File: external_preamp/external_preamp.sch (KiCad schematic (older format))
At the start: 2 parts

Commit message: Monday night hacking
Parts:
- added C1, C7: 0.68uF, symbol Device:C
- added C10, C3: 4.7uF, symbol Device:C
- added C11, C4: 25uF, symbol Device:C
- added C12, C20, C21, C5: 0.022uF, symbol Device:C
- added C13, C15, C17, C18: 220uF 450V, symbol Device:C
- added C14, C6: 47uF 450V, symbol Device:CP
- added C16: C, symbol Device:C
- added C19: 470pF, symbol Device:C
- added C2, C9: 1uF, symbol Device:C
- added C22: 0.1uF, symbol Device:C
- added C8: 0.01uF, symbol Device:C
- added D1, D2, D4, D5: 1N4007, symbol pspice:DIODE
- added D3: LED, symbol Device:LED
- added F1: F1494-ND, symbol Device:Fuse
- added J1: IEC_SOCKET, symbol yga1:IEC_SOCKET
- added J2: IN, symbol yga1:jack_0.25in_mono_sw
- added J3: OUT, symbol yga1:jack_0.25in_mono_sw
- added R10: 10K 1W, symbol Device:R
- added R11: 3K 2W, symbol Device:R
- added R12, R4, R6, R9: 220K, symbol Device:R
- added R13, R15, R18, R2, R20, R7: 100K, symbol Device:R
- added R14, R19, R3, R8: 820, symbol Device:R
- added R16: 100K 2W, symbol Device:R
- added R17: 33K, symbol Device:R
- added R5: R, symbol Device:R
- added RV1, RV4: 100K, symbol Device:R_POT
- added RV10, RV8: 1M LOG, symbol Device:R_POT
- added RV2, RV5: 5K, symbol Device:R_POT
- added RV3, RV6: 500K LOG, symbol Device:R_POT
- added RV7: 250K LN, symbol Device:R_POT
- added RV9: 100K LN, symbol Device:R_POT
- added SW1: EG4810-ND, symbol Switch:SW_SPST
- added SW2, SW4: SW_SP4T, symbol yga1:SW_SP4T
- added SW3, SW5: SW_SPST, symbol Switch:SW_SPST
- added T1: HM4995-ND, symbol Device:Transformer_1P_2S
- added unit 2 of V1
- added V2, V3: 12AX7A, symbol external_preamp-rescue:12AX7A
- R1: renamed from R?; value R -> 1M; symbol R -> external_preamp-rescue:R
- V1: renamed from V?; symbol 12AX7A -> external_preamp-rescue:12AX7A
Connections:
- net Earth: now also C1.2, C10.2, C11.2, C13.2, C14.2, C15.2, C17.2, C18.2, C2.2, C3.2, C4.2, C6.2, C7.2, C9.2, J1.2 (G), J2.2, J2.3, J3.2, R12.1, R14.2, R15.2, R16.2, R19.2, R20.2, R3.2, R6.1, R8.2, RV10.3, RV3.3, RV6.3, RV9.3
- net at V1.1-UA (A): now also C5.2, R2.2
- net at V1.2-UA (G): now also R1.1, J2.1
- net at V1.3-UA (C): now also RV2.1, SW2.A
- net lf1: now reaches V1.4-UA
- net f2: now reaches V1.9
- net f2: now also D3.1 (K), T1.6 (SD), V1.9, V2.9, V2.9, V3.9, V3.9
- new net: C4.1, SW2.1
- new net: R3.1, RV2.2, RV2.3
- new net: C12.2, R7.2, V1.6-UB (A)
- new net: C8.1, R4.1, R6.2, V1.7-UB (G)
- new net: RV5.1, SW4.A, V1.8-UB (C)
- new net: R13.2, V2.1-UA (A), V2.7-UB (G)
- new net: C16.1, R12.2, R9.1, V2.2-UA (G)
- new net: R14.1, V2.3-UA (C)
- new net: C19.2, R15.1, R17.1, V2.8-UB (C)
- new net: C5.1, RV3.1
- new net: R4.2, RV3.2, SW3.1 (A)
- new net: R2.1, RV1.2, RV1.3
- new net: C3.1, SW2.2
- new net: C2.1, SW2.3
- new net: C1.1, SW2.4
- new net: C14.1, C6.1, R10.2, RV1.1, RV4.1
- new net: C8.2, SW3.2 (B)
- new net: C11.1, SW4.1
- new net: R8.1, RV5.2, RV5.3
- new net: C12.1, RV6.1
- new net: R9.2, RV6.2, SW5.1 (A)
- new net: R7.1, RV4.2, RV4.3
- new net: C10.1, SW4.2
- new net: C9.1, SW4.3
- new net: C7.1, SW4.4
- new net: C16.2, SW5.2 (B)
- new net: C19.1, RV7.1
- new net: C20.2, C21.2, R17.2
- new net: RV10.1, RV7.2
- new net: C20.1, RV7.3, RV8.1, RV8.2
- new net: RV8.3, RV9.1
- new net: C21.1, RV9.2
- new net: R18.2, V3.1-UA (A), V3.7-UB (G)
- new net: R19.1, V3.3-UA (C)
- new net: C22.2, R20.1, V3.8-UB (C)
- new net: C22.1, J3.1
- new net: J1.1 (L), SW1.1 (A)
- new net: J1.3 (N), T1.2 (AB)
- new net: F1.2, SW1.2 (B)
- new net: F1.1, T1.1 (AA)
- new net: D1.2 (A), D4.1 (K), T1.3 (SA)
- new net: D2.2 (A), D5.1 (K), T1.4 (SB)
- new net: D1.1 (K), D2.1 (K)
- new net: C13.1, C15.1, D4.2 (A), D5.2 (A), R11.2
- new net: C17.1, C18.1, R11.1, R16.1
- new net: D3.2 (A), R5.2
- new net B+: R10.1, R13.1, R18.1, V2.6-UB (A), V3.6-UB (A)
- new net f1: R5.1, T1.5 (SC), V1.5-UB, V2.4-UA, V2.5-UB, V3.4-UA, V3.5-UB
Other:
- note added: "300V"
- note added: "6.3V"
- moved on the sheet: R1, V1A

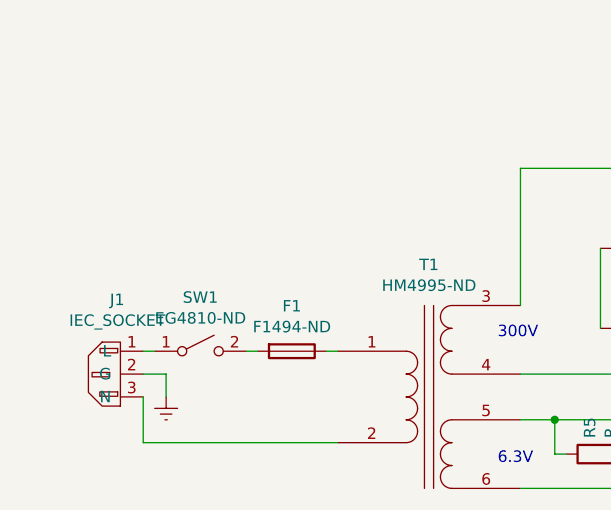
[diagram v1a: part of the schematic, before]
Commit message: schematic and analysis for ax84 preamp mod
Replacing the two separate inputs with a single two stage input to attempt to get nice overdrive tones.
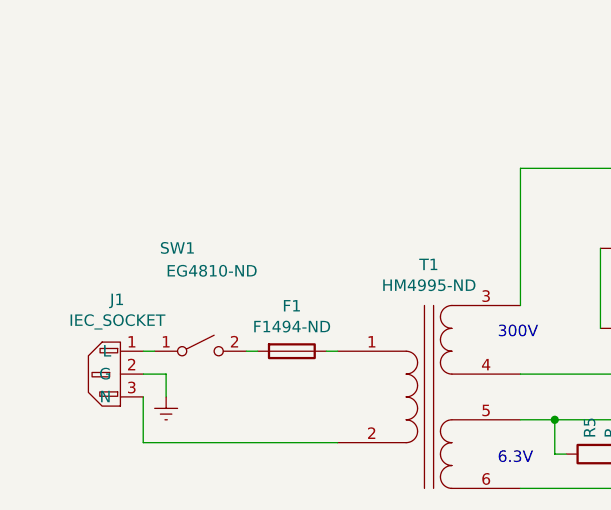
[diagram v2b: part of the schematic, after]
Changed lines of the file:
@@
 U 1 1 5CB3CFE6
 P 1250 6300
-F 0 "SW1" H 1250 6535 50  0000 C CNN
-F 1 "EG4810-ND" H 1250 6444 50  0000 C CNN
+F 0 "SW1" H 1150 6750 50  0000 C CNN
+F 1 "EG4810-ND" H 1300 6650 50  0000 C CNN
 F 2 "" H 1250 6300 50  0001 C CNN
 F 3 "" H 1250 6300 50  0001 C CNN
